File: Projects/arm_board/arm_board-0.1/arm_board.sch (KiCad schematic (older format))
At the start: 1 part

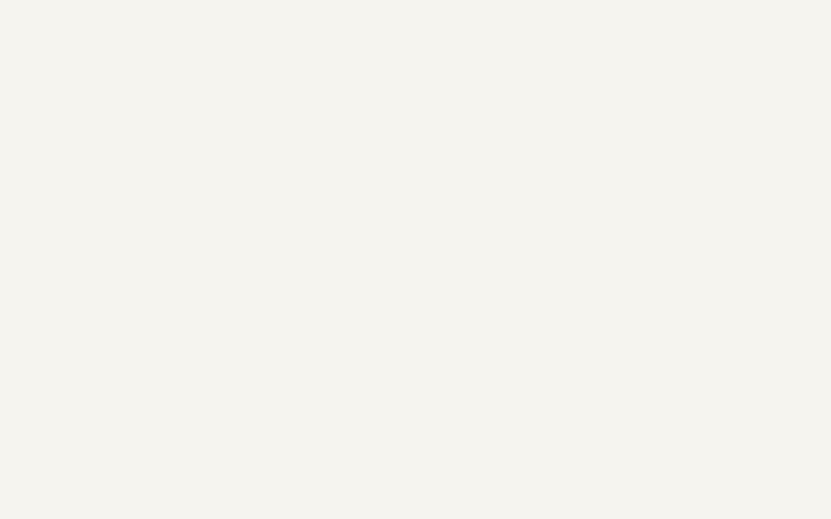
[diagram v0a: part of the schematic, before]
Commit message: Arm Board: Add selector for quadrature encoders
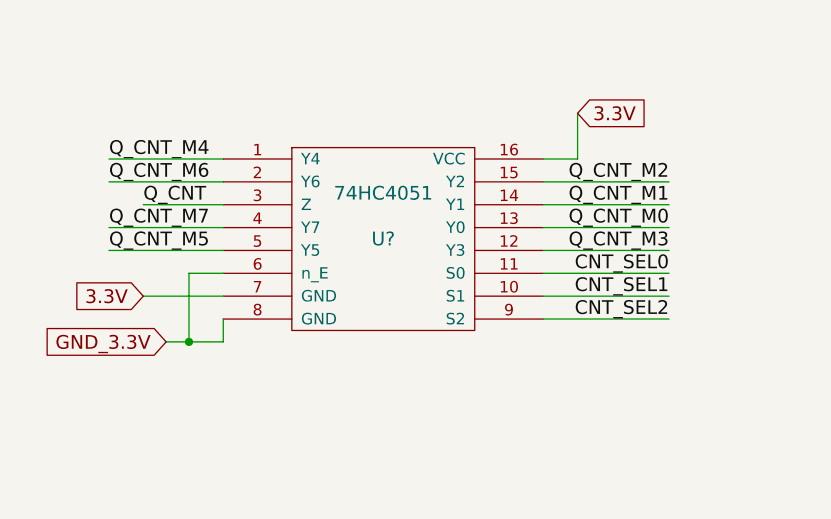
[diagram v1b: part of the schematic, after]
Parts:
- added U?: 74HC4051, symbol 74HC4051
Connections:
- net Q_CNT_M0: now also U?.13 (Y0)
- net Q_CNT_M1: now also U?.14 (Y1)
- net Q_CNT_M2: now also U?.15 (Y2)
- net Q_CNT_M3: now also U?.12 (Y3)
- net Q_CNT_M4: now also U?.1 (Y4)
- net Q_CNT_M5: now also U?.5 (Y5)
- new net 3.3V: U?.16 (VCC), U?.7 (GND)
- new net CNT_SEL0: U?.11 (S0)
- new net CNT_SEL1: U?.10 (S1)
- new net CNT_SEL2: U?.9 (S2)
- new net GND_3.3V: U?.6 (n_E), U?.8 (GND)
- new net Q_CNT: U?.3 (Z)
- new net Q_CNT_M6: U?.2 (Y6)
- new net Q_CNT_M7: U?.4 (Y7)

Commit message: Arm Board: Added multiplexers for underflow/overflow signals on motors.
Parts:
- added P?: CONN_20X2, ~, symbol CONN_20X2
- added U? (x2): 74HC4051, symbol 74HC4051
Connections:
- net labels added: MCU_PWM0, MCU_PWM1, MCU_PWM2, MCU_PWM3, MCU_PWM4, MCU_PWM5, MCU_PWM6, MCU_PWM7, MCU_SCLK, MCU_SDI, MCU_SDO, MTR_CLR, MTR_DATA, MTR_EN, MTR_SEL0, MTR_SEL1, MTR_SEL2, OVRFLW, OVRFLW_SEL0, OVRFLW_SEL1, OVRFLW_SEL2, UDRFLW, UDRFLW_SEL0, UDRFLW_SEL1, UDRFLW_SEL2, Whiper_GND, Whiper_V++
- wire segments 127 -> 224
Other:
- moved on the sheet: U?

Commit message: Arm Board: Finish schematic
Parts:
- removed P?: CONN_20X2, ~, symbol CONN_20X2
- added P?: CONN_25X2, ~, symbol CONN_25X2
- added P? (x2): CONN_2, ~, symbol CONN_2
- added U?: 7805, ~, symbol 7805
- gave numbers to parts that had none: 1
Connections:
- net labels added: 12V, EOC_MCU, GND_12V, MCU_FS, NOISE_5V, NOISE_GND_5V, WIPER_2, n_ADC_CS, n_ADC_CSTART
- wire segments 224 -> 236

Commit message: Arm Board: added reset lines and fixed various errors
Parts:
- removed P?: CONN_25X2, ~, symbol CONN_25X2
- added DEMUX: 74HC138, symbol 74HC138
- added P?: CONN_12X2, ~, symbol CONN_12X2
- added P?: CONN_6X2, ~, symbol CONN_6X2
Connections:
- net labels added: RST, SEL0, SEL1, SEL2, Whiper_0, Whiper_1, Whiper_2
- net labels removed: CNT_SEL0, CNT_SEL1, CNT_SEL2, MTR_SEL0, MTR_SEL1, MTR_SEL2, M_EN, OVRFLW_SEL0, OVRFLW_SEL1, OVRFLW_SEL2, PWM_M0, PWM_M1, UDRFLW_SEL0, UDRFLW_SEL1, UDRFLW_SEL2
- wire segments 236 -> 248
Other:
- moved on the sheet: MUX

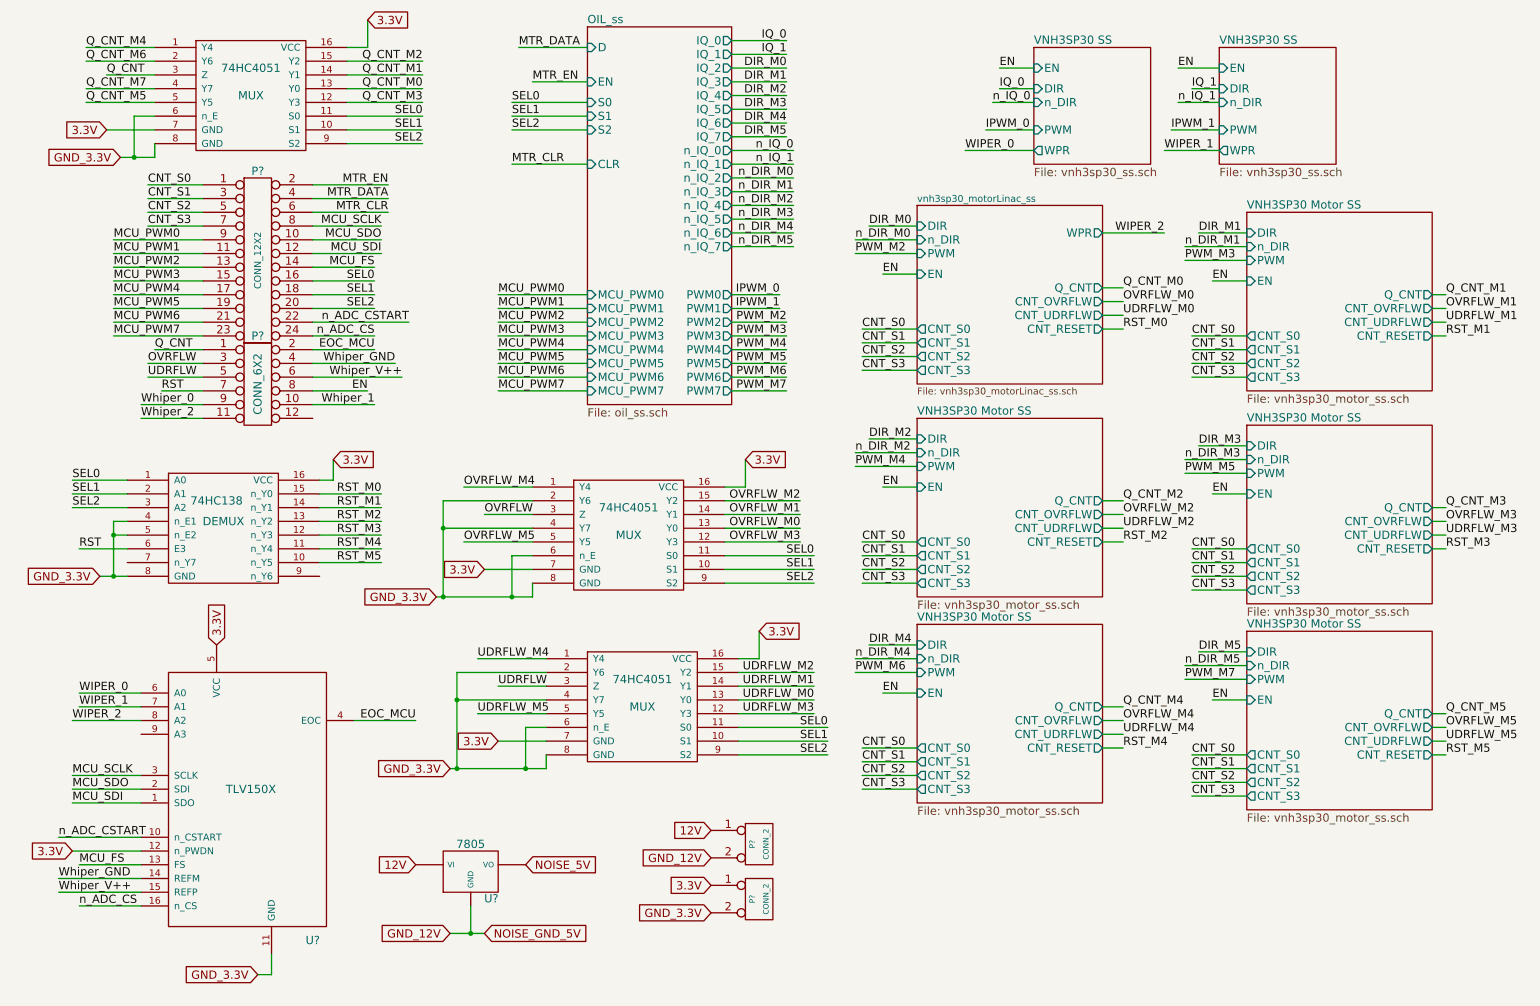
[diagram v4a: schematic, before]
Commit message: Arm Board: bug fixes, and added footprints
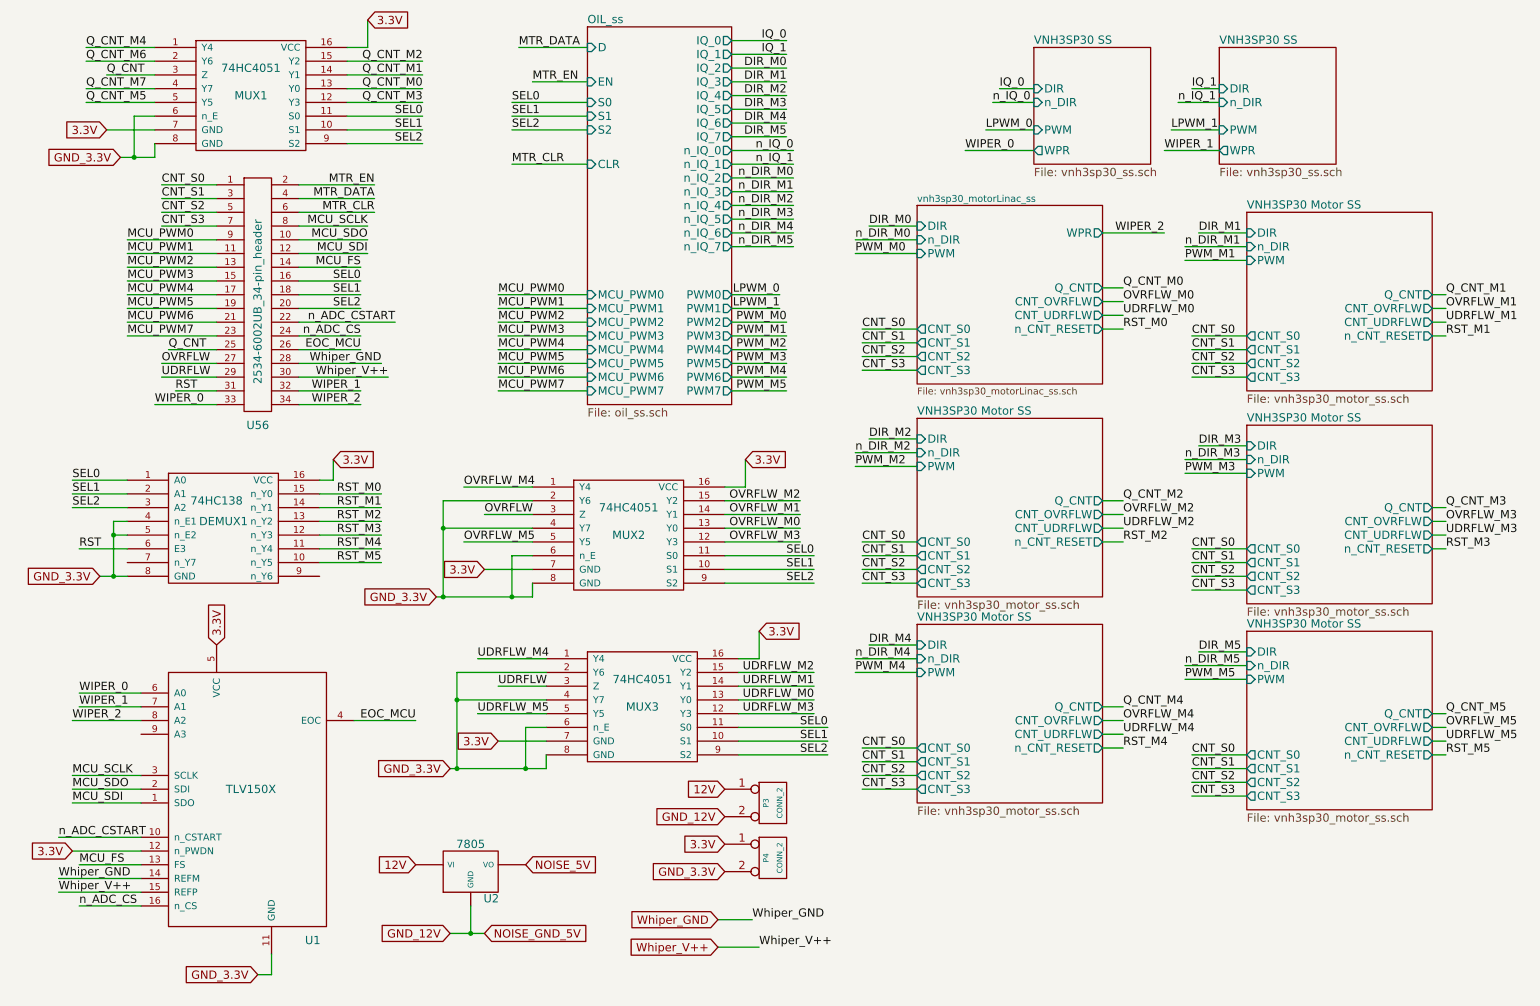
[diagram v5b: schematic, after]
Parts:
- removed P?: CONN_12X2, ~, symbol CONN_12X2
- removed P?: CONN_6X2, ~, symbol CONN_6X2
- added U56: 2534-6002UB_34-pin_header, ArmFootprints:34-pin_2534-6002UB, symbol 2534-6002UB_34-pin_header
- DEMUX1: renamed from DEMUX; footprint (none) -> SMD_Packages:SO-16-N
- MUX1, MUX2, MUX3: renamed from MUX; footprint (none) -> SMD_Packages:SO-16-N
- P3, P4: renamed from P?; footprint ~ -> ArmFootprints:MiniFitJr_2-pin_0039310028
- U1: renamed from U?; footprint (none) -> SMD_Packages:SO-16-N
- U2: renamed from U?; footprint ~ -> ArmFootprints:MC7805CDTRKG
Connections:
- net CNT_S0: now also U56.1
- net CNT_S1: now also U56.3
- net CNT_S2: now also U56.5
- net CNT_S3: now also U56.7
- net EOC_MCU: now also U56.26
- net MCU_FS: now also U56.14
- net MCU_PWM0: now also U56.9
- net MCU_PWM1: now also U56.11
- net MCU_PWM2: now also U56.13
- net MCU_PWM3: now also U56.15
- net MCU_PWM4: now also U56.17
- net MCU_PWM5: now also U56.19
- net MCU_PWM6: now also U56.21
- net MCU_PWM7: now also U56.23
- net MCU_SCLK: now also U56.8
- net MCU_SDI: now also U56.12
- net MCU_SDO: now also U56.10
- net MTR_CLR: now also U56.6
- net MTR_DATA: now also U56.4
- net MTR_EN: now also U56.2
- net OVRFLW: now also U56.27
- net Q_CNT: now also U56.25
- net RST: now also U56.31
- net SEL0: now also U56.16
- net SEL1: now also U56.18
- net SEL2: now also U56.20
- net UDRFLW: now also U56.29
- net WIPER_0: now also U56.33
- net WIPER_1: now also U56.32
- net WIPER_2: now also U56.34
- net Whiper_GND: now also U56.28
- net Whiper_V++: now also U56.30
- net n_ADC_CS: now also U56.24
- net n_ADC_CSTART: now also U56.22
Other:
- moved on the sheet: P3, P4

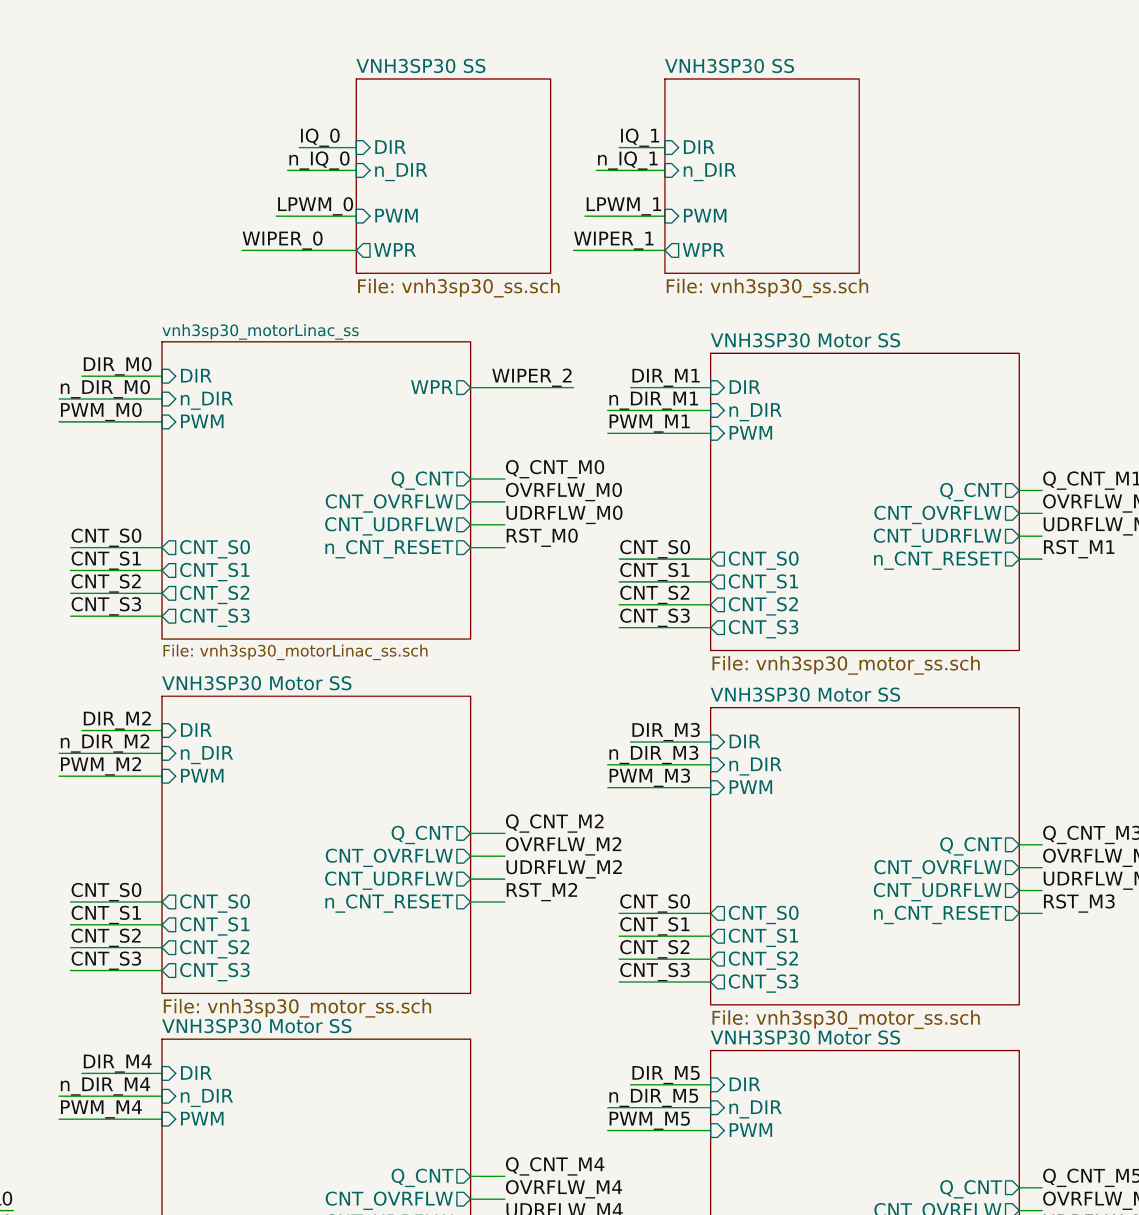
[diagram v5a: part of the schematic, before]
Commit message: Arm Board: bug fixes, cleanup, and start PCB layout
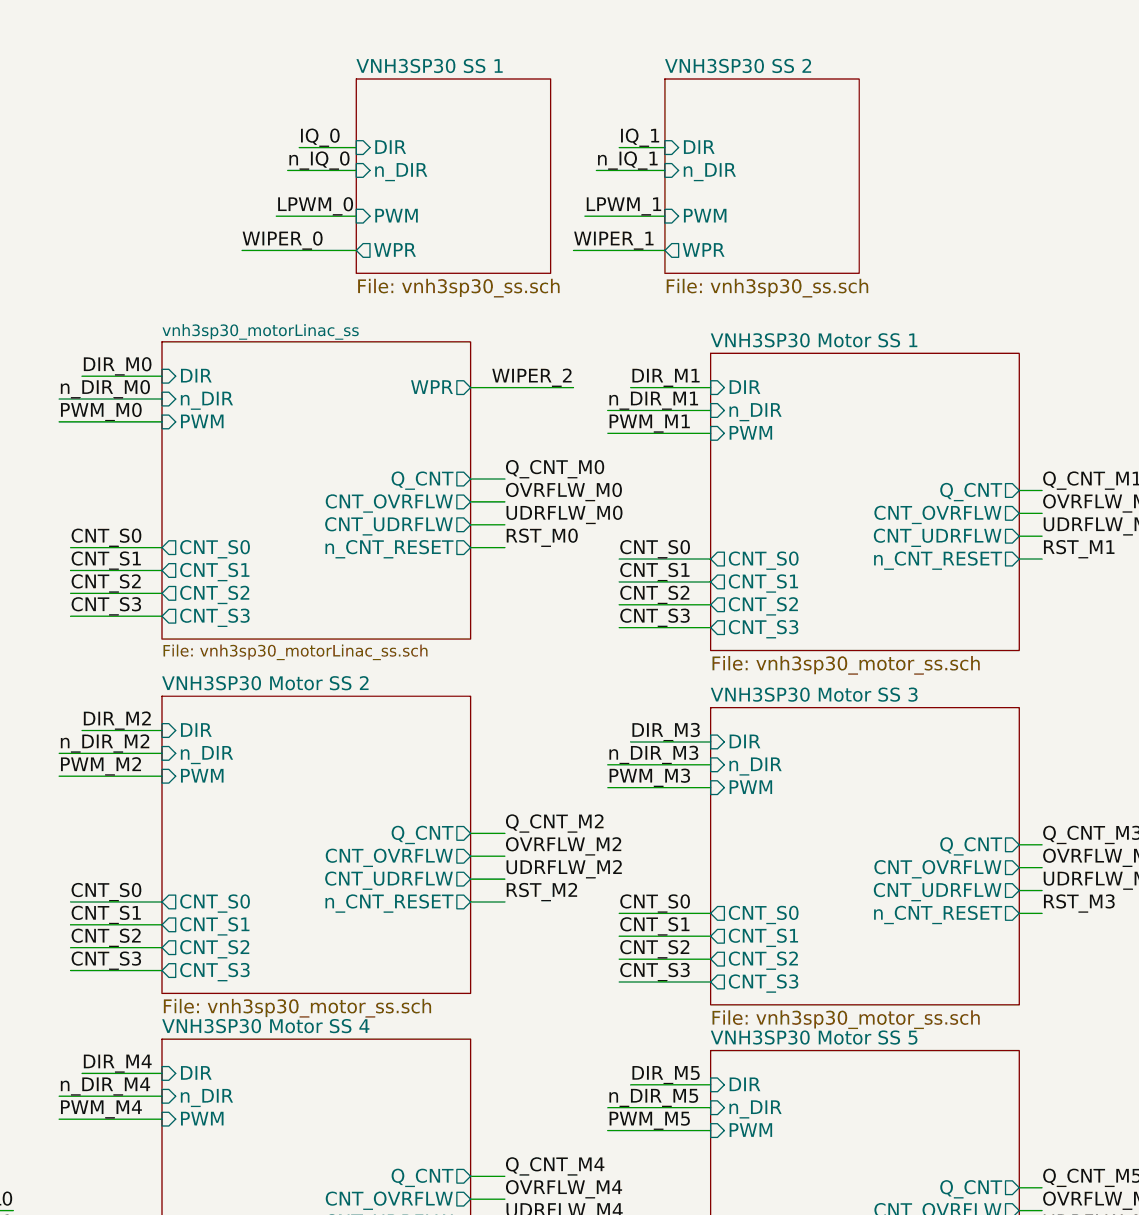
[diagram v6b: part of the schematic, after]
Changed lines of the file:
@@
 S 7800 850  850  850
 U 56458E25
-F0 "VNH3SP30 SS" 60
+F0 "VNH3SP30 SS 1" 60
 F1 "vnh3sp30_ss.sch" 60
 F2 "PWM" I L 7800 1450 60
@@
 S 9150 850  850  850
 U 5645B857
-F0 "VNH3SP30 SS" 60
+F0 "VNH3SP30 SS 2" 60
 F1 "vnh3sp30_ss.sch" 60
 F2 "PWM" I L 9150 1450 60
@@
 S 9350 2050 1350 1300
 U 56F5245F
-F0 "VNH3SP30 Motor SS" 60
+F0 "VNH3SP30 Motor SS 1" 60
 F1 "vnh3sp30_motor_ss.sch" 60
 F2 "DIR" I L 9350 2200 60
@@
 S 9350 3600 1350 1300
 U 56F544AF
-F0 "VNH3SP30 Motor SS" 60
+F0 "VNH3SP30 Motor SS 3" 60
 F1 "vnh3sp30_motor_ss.sch" 60
 F2 "DIR" I L 9350 3750 60
@@
 S 9350 5100 1350 1300
 U 56F55E0D
-F0 "VNH3SP30 Motor SS" 60
+F0 "VNH3SP30 Motor SS 5" 60
 F1 "vnh3sp30_motor_ss.sch" 60
 F2 "DIR" I L 9350 5250 60
@@
 S 6950 5050 1350 1300
 U 56F56B2F
-F0 "VNH3SP30 Motor SS" 60
+F0 "VNH3SP30 Motor SS 4" 60
 F1 "vnh3sp30_motor_ss.sch" 60
 F2 "DIR" I L 6950 5200 60
@@
 Text Label 800  5750 0    60   ~ 0
 WIPER_2
-$Comp
-L 7805 U2
-U 1 1 56FC0560
-P 3700 6850
-F 0 "U2" H 3850 6654 60  0000 C CNN
-F 1 "7805" H 3700 7050 60  0000 C CNN
-F 2 "ArmFootprints:MC7805CDTRKG" H 3700 6850 60  0001 C CNN
-F 3 "~" H 3700 6850 60  0000 C CNN
-	1    3700 6850
-	1    0    0    -1
-$EndComp
 Text GLabel 3300 6800 0    60   Input ~ 0
 12V
@@
 S 6950 3550 1350 1300
 U 56F53B7D
-F0 "VNH3SP30 Motor SS" 60
+F0 "VNH3SP30 Motor SS 2" 60
 F1 "vnh3sp30_motor_ss.sch" 60
 F2 "DIR" I L 6950 3700 60
@@
 	1    0    0    -1
 $EndComp
+$Comp
+L 7805 U2
+U 1 1 56C90A98
+P 3700 6850
+F 0 "U2" H 3850 6654 60  0000 C CNN
+F 1 "7805" H 3700 7050 60  0000 C CNN
+F 2 "ArmFootprints:MC7805CDTRKG" H 3700 6850 60  0001 C CNN
+F 3 "" H 3700 6850 60  0000 C CNN
+	1    3700 6850
+	1    0    0    -1
+$EndComp
